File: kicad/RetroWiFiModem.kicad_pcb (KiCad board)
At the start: 2 copper layers, 102.5 x 66.1 mm, 38 parts, among them CON1 BARREL_JACK, P1 CONN_02X05, U1 74HC245, U2 MAX3232, U3 74HC32, U4 LP2950ACZ-3.3, U5 WeMos_D1_mini

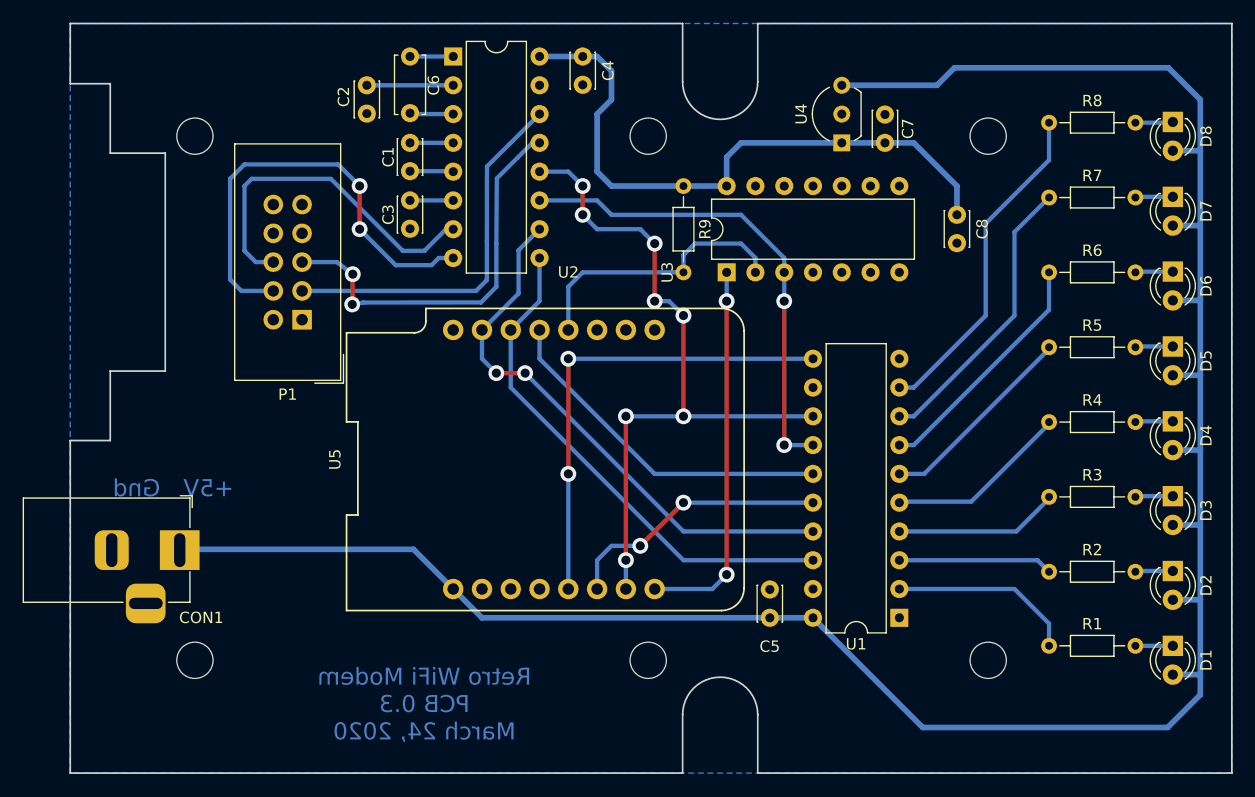
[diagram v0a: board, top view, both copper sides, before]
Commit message: Initial commit for the v2 hardware. * MAX3237 for full suite of RS-232 control signals * DFPlayer Mini for faux dialing and connection sounds * Gerbers suitable for JLCPCB included
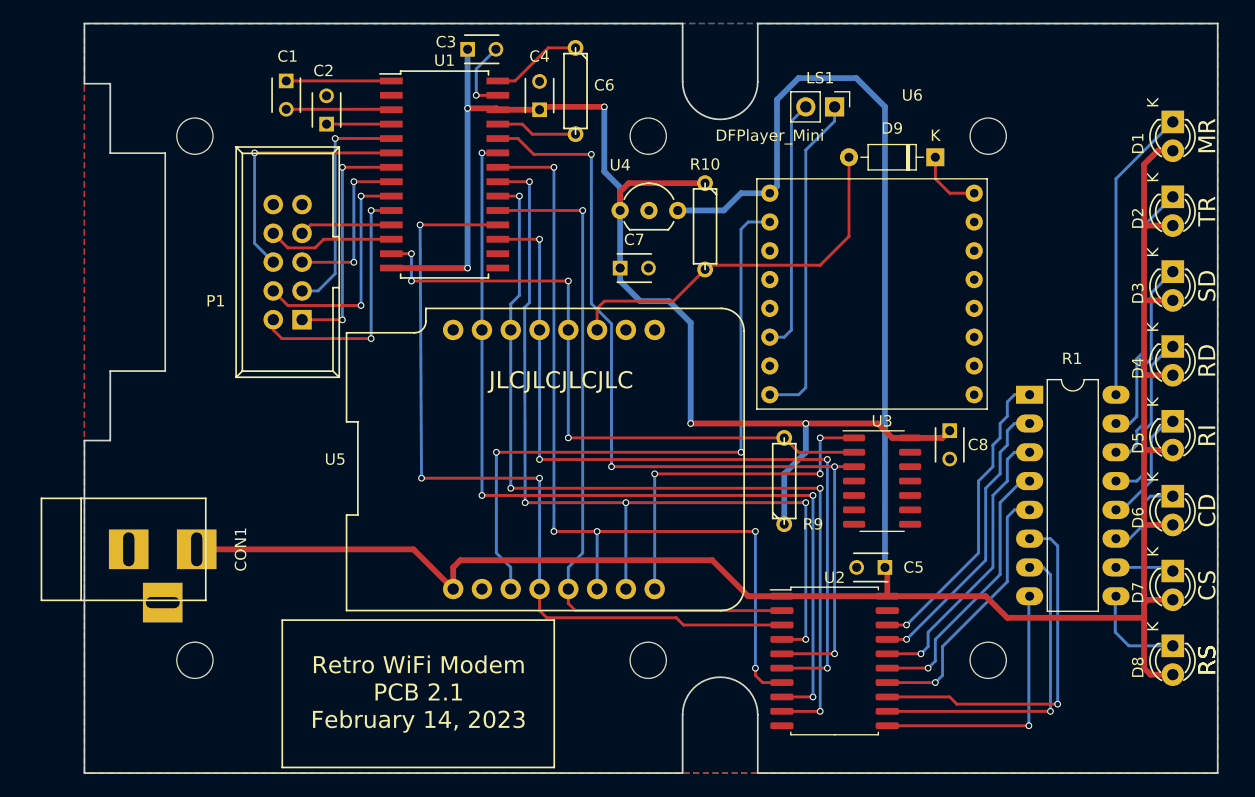
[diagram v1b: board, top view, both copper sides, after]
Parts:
- removed H1, H2, H3, H4, H5, H6: MountingHole, MountingHole:MountingHole_3.2mm_M3
- removed R2, R3, R4, R5, R6, R7, R8: 560R, Resistor_THT:R_Axial_DIN0204_L3.6mm_D1.6mm_P7.62mm_Horizontal
- added ?: , modules:MountingHole_3.2mm_Hammond_1593, F.Cu at (119.5, 85.8)
- added ?: , modules:MountingHole_3.2mm_Hammond_1593, F.Cu at (119.5, 132.0)
- added ?: , modules:MountingHole_3.2mm_Hammond_1593, F.Cu at (159.4, 132.0)
- added ?: , modules:MountingHole_3.2mm_Hammond_1593, F.Cu at (159.4, 85.8)
- added ?: , modules:MountingHole_3.2mm_Hammond_1593, F.Cu at (189.4, 85.8)
- added ?: , modules:MountingHole_3.2mm_Hammond_1593, F.Cu at (189.4, 132.0)
- added D9: 1N4148, modules:D_DO-35_SOD27_P7.62mm_Horizontal, F.Cu at (184.8, 87.6)
- added LS1: Speaker, modules:PinHeader_1x02_P2.54mm_Vertical, F.Cu at (175.9, 83.2)
- added R10: 10K, modules:R3, F.Cu at (164.5, 93.7)
- added U6: DFPlayer_Mini, modules:DFPlayerMini, F.Cu at (170.2, 90.8)
- C1, C2, C3, C4, C5, C7, C8: footprint Capacitor_THT:C_Disc_D3.0mm_W2.0mm_P2.50mm -> modules:C_Disc_D3_P2.5
- C6: footprint Capacitor_THT:C_Disc_D5.0mm_W2.5mm_P5.00mm -> modules:R3
- CON1: value BARREL_JACK -> 5V centre +; footprint Connector_BarrelJack:BarrelJack_Horizontal -> modules:BARREL_JACK
- D1, D2, D3, D4, D5, D6, D7, D8: footprint LED_THT:LED_D3.0mm -> modules:LED-3MM
- P1: footprint Connector_IDC:IDC-Header_2x05_P2.54mm_Vertical -> modules:IDC_Header_Straight_10pins
- R1: footprint Resistor_THT:R_Axial_DIN0204_L3.6mm_D1.6mm_P7.62mm_Horizontal -> modules:DIP-16_W7.62mm_LongPads
- R9: footprint Resistor_THT:R_Axial_DIN0204_L3.6mm_D1.6mm_P7.62mm_Horizontal -> modules:R3
- U1: value 74HC245 -> MAX3237CAI+; footprint Package_DIP:DIP-20_W7.62mm -> modules:SOIC-28W_7.5x17.9mm_Pitch1.27mm
- U2: value MAX3232 -> 74HCT245; footprint Package_DIP:DIP-16_W7.62mm -> modules:SOIC-20W_7.5x12.8mm_P1.27mm
- U3: footprint Package_DIP:DIP-14_W7.62mm -> modules:SOIC-14_3.9x8.7mm_P1.27mm
- U4: value LP2950ACZ-3.3 -> L4931CZ33-AP; footprint Package_TO_SOT_THT:TO-92L_Inline_Wide -> modules:TO-92_Inline_Wide
- U5: value WeMos_D1_mini -> WeMos_mini; footprint RetroWiFiModem-footprints:wemos-d1-mini -> modules:wemos-d1-mini-with-pin-header-and-connector
- moved U2 63.1 mm to (175.9, 132.1)
- moved U1 56.0 mm to (141.5, 89.2), turned to 0 degrees
- moved D1 46.2 mm to (205.7, 84.5)
- moved D8 46.2 mm to (205.7, 130.7)
- moved D2 33.0 mm to (205.7, 91.1)
- moved D7 33.0 mm to (205.7, 124.1)
- moved R9 27.5 mm to (171.4, 116.2), turned to 90 degrees
- moved C7 25.8 mm to (157.0, 97.4), turned to 0 degrees
- moved U3 23.0 mm to (180.1, 116.2), turned to 0 degrees
- moved R1 22.2 mm to (193.1, 108.6)
- moved U4 20.4 mm to (157.0, 92.3), turned to 0 degrees
- moved D3 19.8 mm to (205.7, 97.7)
- moved D6 19.8 mm to (205.7, 117.5)
- moved C8 19.1 mm to (186.1, 111.8)
- moved C6 14.9 mm to (153.0, 81.8)
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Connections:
- C3 pad 1: Net-(C3-Pad1) -> +3V3
- C3 pad 2: GND -> Net-(C3-Pad2)
- R1 pad 2: Net-(D1-Pad1) -> Net-(R1-Pad2)
- U1 pad 1: GND -> Net-(C1-Pad1)
- U1 pad 10: GND -> Net-(P1-Pad2)
- U1 pad 11: Net-(U1-Pad11) -> Net-(P1-Pad7)
- U1 pad 12: GND -> Net-(P1-Pad8)
- U1 pad 13: Net-(U1-Pad13) -> Net-(R9-Pad2)
- U1 pad 14: Net-(U1-Pad14) -> +3V3
- U1 pad 15: Net-(U1-Pad15) -> GND
- U1 pad 19: GND -> Net-(U1-Pad19)
- U1 pad 2: Net-(R1-Pad1) -> GND
- U1 pad 20: +5V -> Net-(U1-Pad20)
- U1 pad 3: Net-(R2-Pad1) -> Net-(C1-Pad2)
- U1 pad 4: Net-(R3-Pad1) -> Net-(C2-Pad1)
- U1 pad 5: Net-(R4-Pad1) -> Net-(P1-Pad3)
- U1 pad 6: Net-(R5-Pad1) -> Net-(P1-Pad6)
- U1 pad 7: Net-(R6-Pad1) -> Net-(P1-Pad1)
- U1 pad 8: Net-(R7-Pad1) -> Net-(P1-Pad5)
- U1 pad 9: Net-(R8-Pad1) -> Net-(P1-Pad4)
- U2 pad 1: Net-(C6-Pad1) -> +5V
- U2 pad 10: Net-(U1-Pad17) -> GND
- U2 pad 11: Net-(U1-Pad14) -> Net-(R1-Pad8)
- U2 pad 12: Net-(U1-Pad13) -> Net-(R1-Pad7)
- U2 pad 13: Net-(P1-Pad5) -> Net-(R1-Pad6)
- U2 pad 14: Net-(P1-Pad3) -> Net-(R1-Pad5)
- U2 pad 15: GND -> Net-(R1-Pad4)
- U2 pad 16: +3V3 -> Net-(R1-Pad3)
- U2 pad 2: Net-(C2-Pad1) -> Net-(U1-Pad19)
- U2 pad 3: Net-(C6-Pad2) -> Net-(U1-Pad18)
- U2 pad 4: Net-(C1-Pad1) -> Net-(U1-Pad21)
- U2 pad 5: Net-(C1-Pad2) -> Net-(U1-Pad24)
- U2 pad 6: Net-(C3-Pad1) -> Net-(U1-Pad17)
- U2 pad 7: Net-(P1-Pad6) -> Net-(U1-Pad22)
- U2 pad 8: Net-(P1-Pad4) -> Net-(U1-Pad23)
- U2 pad 9: Net-(U1-Pad18) -> Net-(U1-Pad20)
- U3 pad 3: Net-(U1-Pad14) -> Net-(U1-Pad24)
- U5 pad 13: Net-(U1-Pad15) -> Net-(U1-Pad17)
- U5 pad 14: Net-(U1-Pad18) -> Net-(U1-Pad20)
- U5 pad 15: Net-(U1-Pad17) -> Net-(U1-Pad23)
- U5 pad 4: Net-(U5-Pad4) -> Net-(U1-Pad18)
- U5 pad 5: Net-(U1-Pad11) -> Net-(U1-Pad19)
- U5 pad 6: Net-(U1-Pad16) -> Net-(U1-Pad22)
- U5 pad 7: Net-(U1-Pad13) -> Net-(U1-Pad21)
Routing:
- net Net-(U1-Pad23): track 0.00 -> 81.4 mm, vias 0 -> 4
- net Net-(U1-Pad24): track 0.00 -> 79.7 mm, vias 0 -> 4
- net Net-(U1-Pad20): track 0.00 -> 78.4 mm, vias 0 -> 4
- net Net-(U1-Pad21): track 0.00 -> 77.8 mm, vias 0 -> 5
- net Net-(U1-Pad22): track 0.00 -> 75.2 mm, vias 0 -> 5
- net Net-(U1-Pad13): track 63.1 -> 0.00 mm, vias 8 -> 0
- net Net-(U1-Pad19): track 0.00 -> 62.0 mm, vias 0 -> 1
- net +3V3: track 55.8 -> 113.6 mm, vias 0 -> 5
- net Net-(U5-Pad3): track 0.00 -> 56.7 mm, vias 0 -> 2
- net Net-(U1-Pad14): track 42.7 -> 0.00 mm, vias 2 -> 0
- net Net-(U1-Pad11): track 41.9 -> 0.00 mm, vias 2 -> 0
- net Net-(D9-Pad2): track 0.00 -> 33.7 mm
- net Net-(R9-Pad2): track 24.6 -> 57.6 mm, vias 0 -> 4
- net Net-(R1-Pad6): track 0.00 -> 32.0 mm, vias 0 -> 1
- net Net-(U1-Pad15): track 30.9 -> 0.00 mm
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- added copper zone on F.Cu, net GND
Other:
- board size 102.5 x 66.1 mm -> 100 x 66.1 mm
- net class Default: trace_width 0.38 -> 0.254; via_dia 1.4 -> 0.6; via_drill 0.9 -> 0.4
- net class Power: clearance 0.3 -> 0.2; trace_width 0.5 -> 0.508; via_dia 1.4 -> 0.6; via_drill 0.9 -> 0.4
- rule pad_to_mask_clearance: 0.2 -> 0
- rule trace_min: 0.38 -> 0.2
- rule via_min_drill: 0.5 -> 0.3
- rule via_min_size: 0.7 -> 0.4
- board text added: "CD"
- board text added: "CS"
- board text added: "JLCJLCJLCJLC"
- board text added: "MR"
- board text added: "RD"
- board text added: "RI"
- board text added: "RS"
- board text added: "Retro WiFi Modem PCB 2.1 February 14, 2023"
- board text added: "SD"
- board text added: "TR"
- board text removed: "Retro WiFi Modem PCB 0.3 March 24, 2020"

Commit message: Completed KiCad 6.0 updates
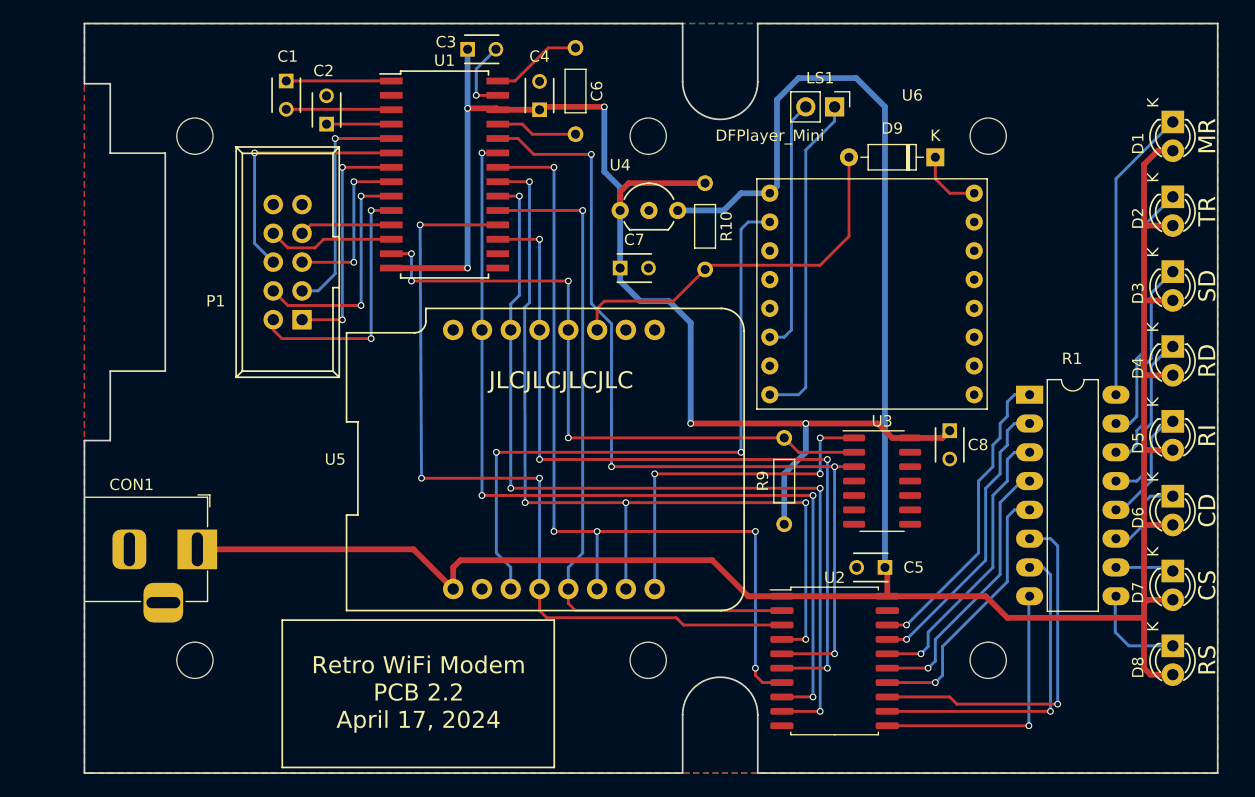
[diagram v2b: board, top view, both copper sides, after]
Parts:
- removed ? (x6): , modules:MountingHole_3.2mm_Hammond_1593
- added H1: MountingHole, footprints:MountingHole_3.2mm, F.Cu at (119.5, 85.8)
- added H2: MountingHole, footprints:MountingHole_3.2mm, F.Cu at (159.4, 85.8)
- added H3: MountingHole, footprints:MountingHole_3.2mm, F.Cu at (189.4, 85.8)
- added H4: MountingHole, footprints:MountingHole_3.2mm, F.Cu at (119.5, 132.0)
- added H5: MountingHole, footprints:MountingHole_3.2mm, F.Cu at (159.4, 132.0)
- added H6: MountingHole, footprints:MountingHole_3.2mm, F.Cu at (189.4, 132.0)
- C6, R10, R9: footprint modules:R3 -> footprints:R3
- CON1: value 5V centre + -> BarrelJack_Horizontal; footprint modules:BARREL_JACK -> footprints:BarrelJack_Horizontal
- moved CON1 6.26 mm to (119.7, 122.2)
- moved C6 3.84 mm to (153.0, 77.9)
- moved R10 3.84 mm to (164.5, 89.9)
- moved R9 3.84 mm to (171.4, 120.0)
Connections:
- CON1 pad 3: Net-(CON1-Pad3) -> unconnected-(CON1-Pad3)
- P1 pad 10: Net-(P1-Pad10) -> unconnected-(P1-Pad10)
- U1 pad 16: Net-(U1-Pad16) -> unconnected-(U1-Pad16)
- U3 pad 11: Net-(U3-Pad11) -> unconnected-(U3-Pad11)
- U3 pad 6: Net-(U3-Pad6) -> unconnected-(U3-Pad6)
- U3 pad 8: Net-(U3-Pad8) -> unconnected-(U3-Pad8)
- U5 pad 10: Net-(U5-Pad10) -> unconnected-(U5-Pad10)
- U5 pad 16: Net-(U5-Pad16) -> unconnected-(U5-Pad16)
- U5 pad 9: Net-(U5-Pad9) -> unconnected-(U5-Pad9)
- U6 pad 11: Net-(U6-Pad11) -> unconnected-(U6-Pad11)
- U6 pad 12: Net-(U6-Pad12) -> unconnected-(U6-Pad12)
- U6 pad 13: Net-(U6-Pad13) -> unconnected-(U6-Pad13)
- U6 pad 14: Net-(U6-Pad14) -> unconnected-(U6-Pad14)
- U6 pad 15: Net-(U6-Pad15) -> unconnected-(U6-Pad15)
- U6 pad 3: Net-(U6-Pad3) -> unconnected-(U6-Pad3)
- U6 pad 4: Net-(U6-Pad4) -> unconnected-(U6-Pad4)
- U6 pad 5: Net-(U6-Pad5) -> unconnected-(U6-Pad5)
- U6 pad 9: Net-(U6-Pad9) -> unconnected-(U6-Pad9)
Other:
- net class Default removed
- net class Power removed
- board text added: "Retro WiFi Modem PCB 2.2 April 17, 2024"
- board text removed: "Retro WiFi Modem PCB 2.1 February 14, 2023"
